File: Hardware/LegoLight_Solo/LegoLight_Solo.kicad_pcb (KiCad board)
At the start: 2 copper layers, 30 x 65 mm, 41 parts, among them IC1 PAM2401SCADJ, J1 USB4105-GF-A, J2 103P012BB100, J3 103P012BB100, J4 Conn_01x02_Socket, J5 VEML7700-TT, J8 I2C, U1 MCP73831-2-OT, U2 KXTJ3-1057

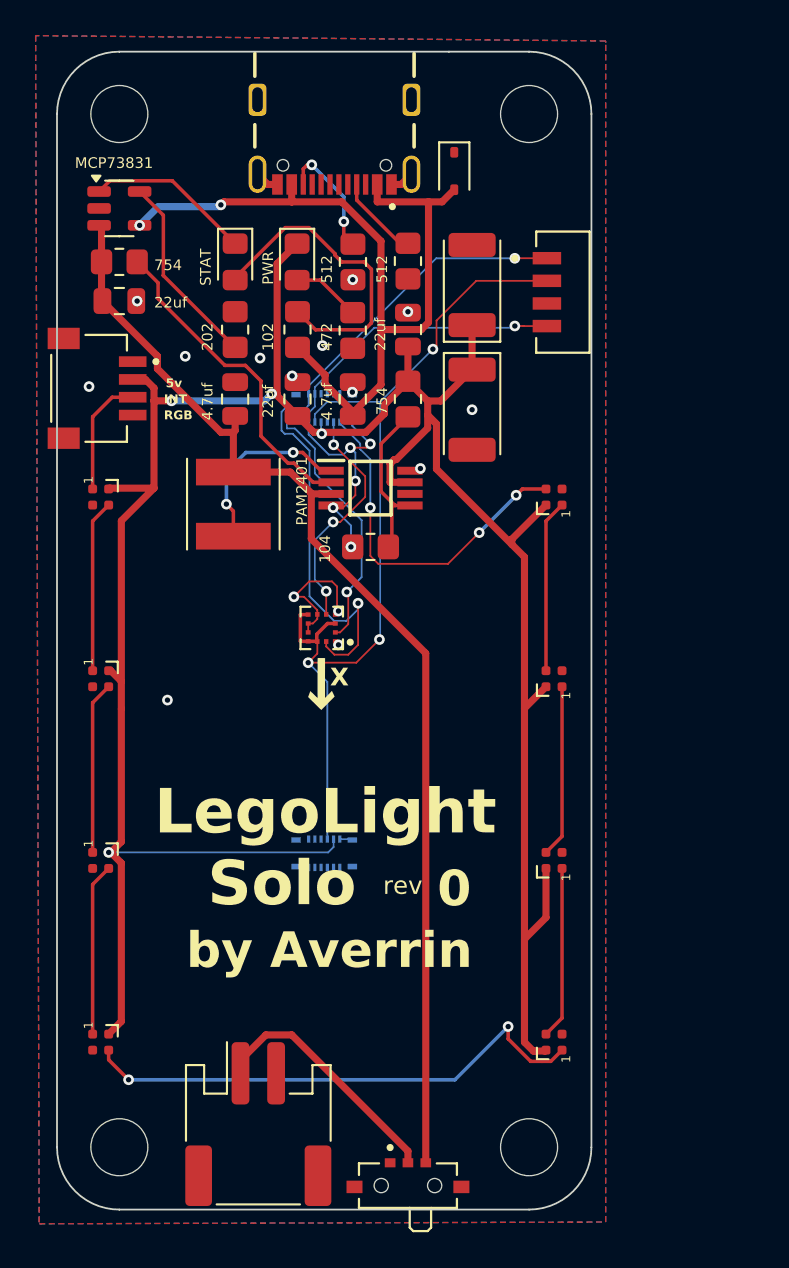
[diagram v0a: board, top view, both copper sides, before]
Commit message: add hq header to solo
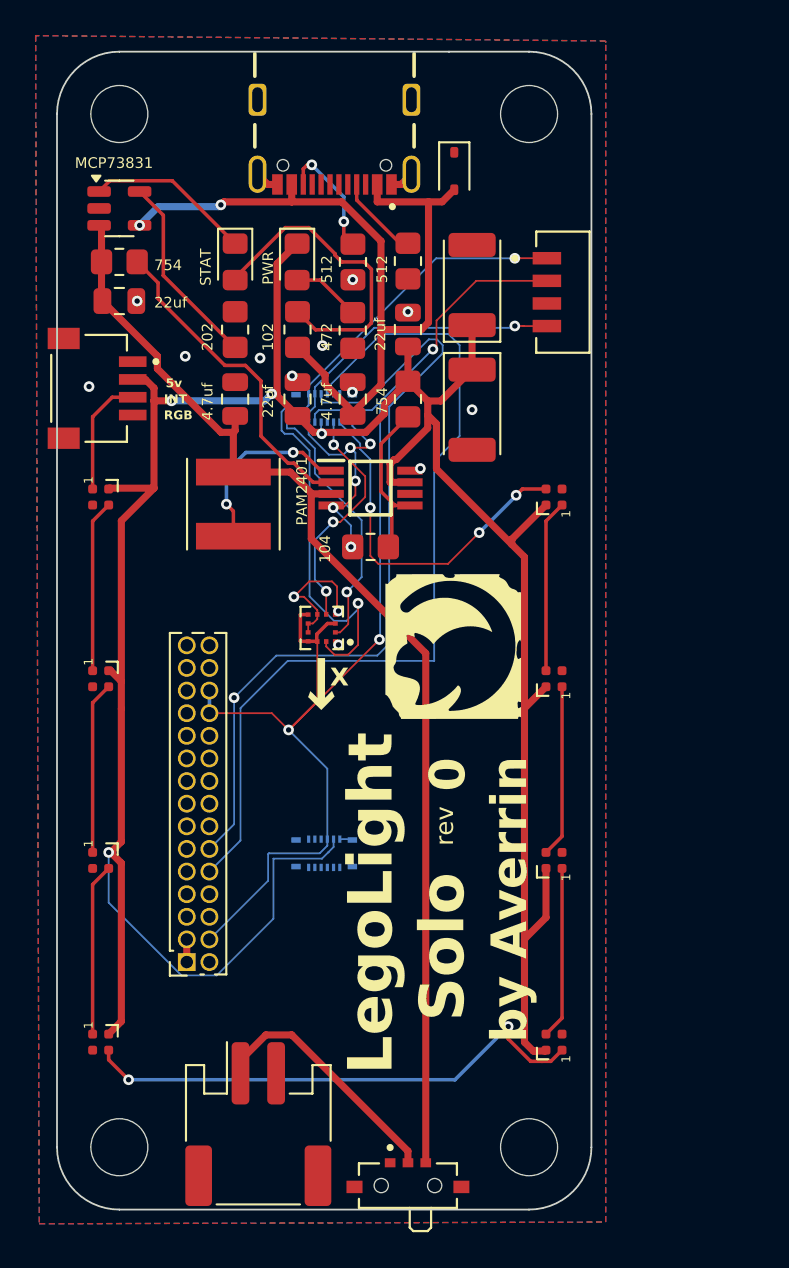
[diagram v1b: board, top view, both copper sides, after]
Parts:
- added J6: Conn_02x15_Counter_Clockwise, Connector_PinSocket_1.27mm:PinSocket_2x15_P1.27mm_Vertical, F.Cu at (67.4, 111.1)
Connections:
- J2 pad 6: unconnected-(J2-Pad6) -> /SDA_ext
- J2 pad 8: unconnected-(J2-Pad8) -> /SCL_ext
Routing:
- net /SDA_ext: track 0.00 -> 49.5 mm
- net /SCL_ext: track 0.00 -> 45.9 mm, vias 0 -> 1
- net +3.3V: track 51.6 -> 71.3 mm
- net +5V: track 146.5 -> 157.2 mm
- net GND: vias 20 -> 19

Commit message: add hq header to solo
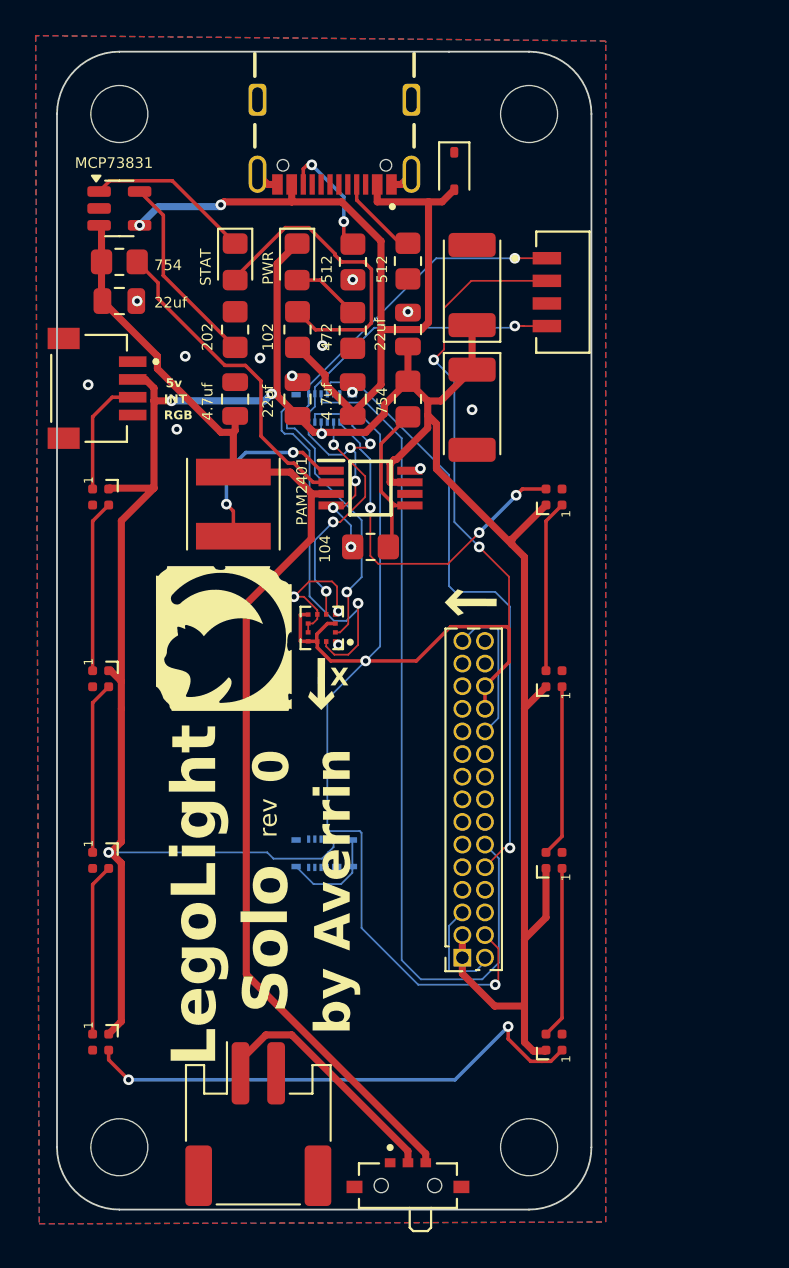
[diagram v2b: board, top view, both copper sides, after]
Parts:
- moved J6 15.5 mm to (82.9, 110.9)
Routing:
- net +3.3V: track 71.3 -> 96.6 mm, vias 3 -> 4
- net GND: track 26.4 -> 46.8 mm, vias 19 -> 20
- net /SDA_ext: track 49.5 -> 35.0 mm, vias 0 -> 1
- net +5V: track 157.2 -> 153.2 mm
- net +BATT: track 64.6 -> 67.6 mm
- net /SCL_ext: track 45.9 -> 48.4 mm, vias 1 -> 0

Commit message: final?
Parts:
- added BTN1: BTN, mouser:B3U-1000P, F.Cu at (88.1, 80.4)
- added J7: Conn_01x02_Socket, Connector_PinHeader_2.54mm:PinHeader_1x02_P2.54mm_Vertical, F.Cu at (68.3, 113.2)
- added R9: 10KOHM, Resistor_SMD:R_0805_2012Metric_Pad1.20x1.40mm_HandSolder, F.Cu at (80.8, 88.7)
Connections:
- J3 pad 1: unconnected-(J3-Pad1) -> /PA07
- J3 pad 3: unconnected-(J3-Pad3) -> /PA06
- J3 pad 5: unconnected-(J3-Pad5) -> /PA05
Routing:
- net /PA05: track 0.00 -> 30.6 mm, vias 0 -> 5
- net Net-(J4-Pin_1): track 14.1 -> 20.4 mm
- net GND: track 46.8 -> 52.5 mm, vias 20 -> 42
- net +3.3V: track 96.6 -> 100.3 mm, vias 4 -> 5
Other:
- board text added: "103"
- board text added: "LegoLight Solo"
- board text removed: "0"
- board text removed: "LegoLight"
- board text removed: "Solo"
- board text removed: "rev"
